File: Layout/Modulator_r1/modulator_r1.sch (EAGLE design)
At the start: 72 parts, among them Q1 FA-20H, U1 ATMEGA328P-AU, U2 TPS79933QDDCRQ1, U3 CC1125RHBT, U4 MCP1700T-3302E/TT, U5 FT232RL, U6 SIP32509DT-T1-GE3

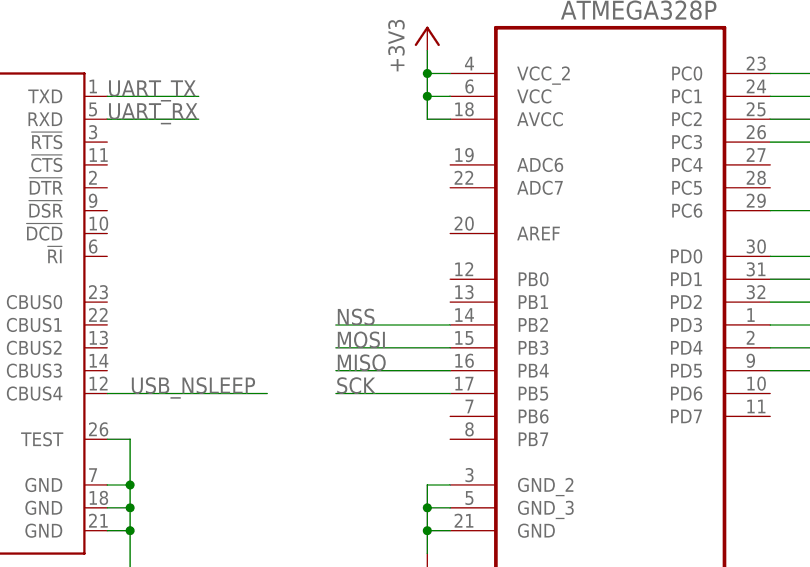
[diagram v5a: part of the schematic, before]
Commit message: Connected CC_Reset and GPIO0.
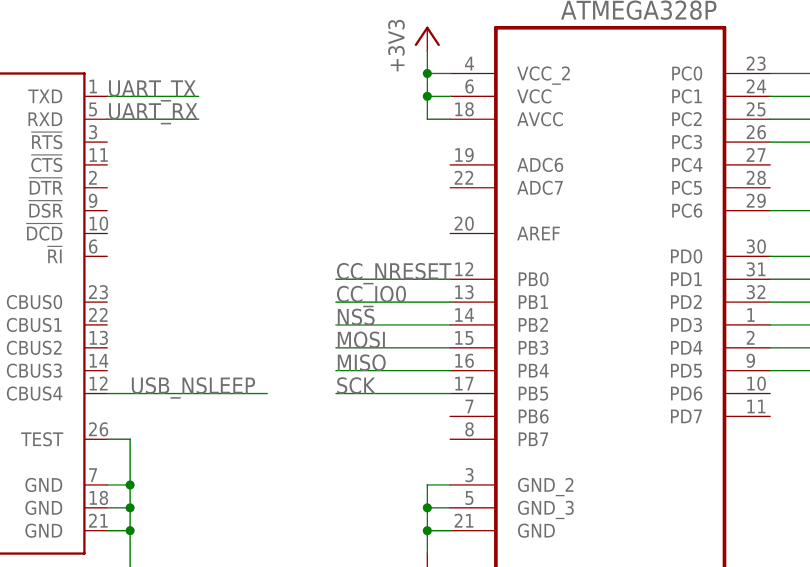
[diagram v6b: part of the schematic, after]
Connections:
- net CC_IO0: now also U1.PB1
- net CC_NRESET: now also U1.PB0
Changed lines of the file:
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@@
 <label x="162.56" y="58.42" size="1.778" layer="95"/>
+</segment>
+<segment>
+<pinref part="U1" gate="A" pin="PB1"/>
+<wire x1="25.4" y1="35.56" x2="12.7" y2="35.56" width="0.1524" layer="91"/>
+<label x="12.7" y="35.56" size="1.778" layer="95"/>
 </segment>
 </net>
@@
 <label x="162.56" y="40.64" size="1.778" layer="95"/>
 </segment>
+<segment>
+<pinref part="U1" gate="A" pin="PB0"/>
+<wire x1="25.4" y1="38.1" x2="12.7" y2="38.1" width="0.1524" layer="91"/>
+<label x="12.7" y="38.1" size="1.778" layer="95"/>
+</segment>
 </net>

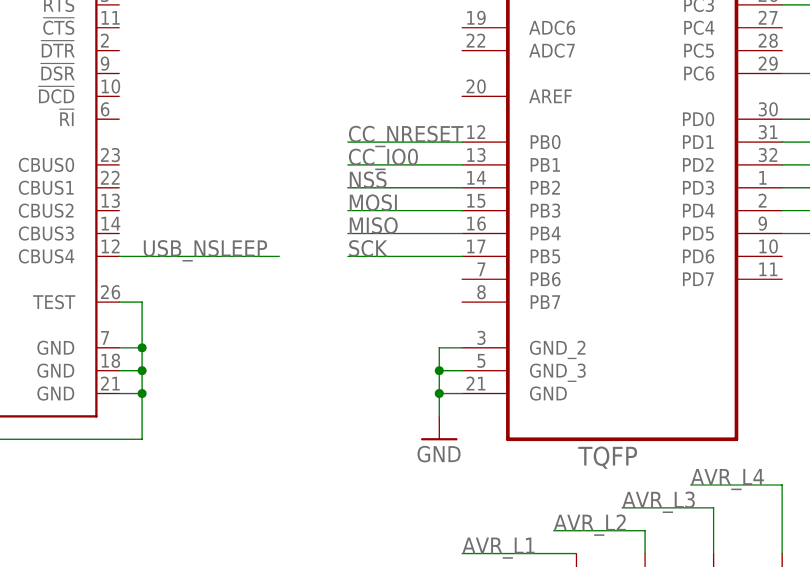
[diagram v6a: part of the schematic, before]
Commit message: Connect GPIO2/3.
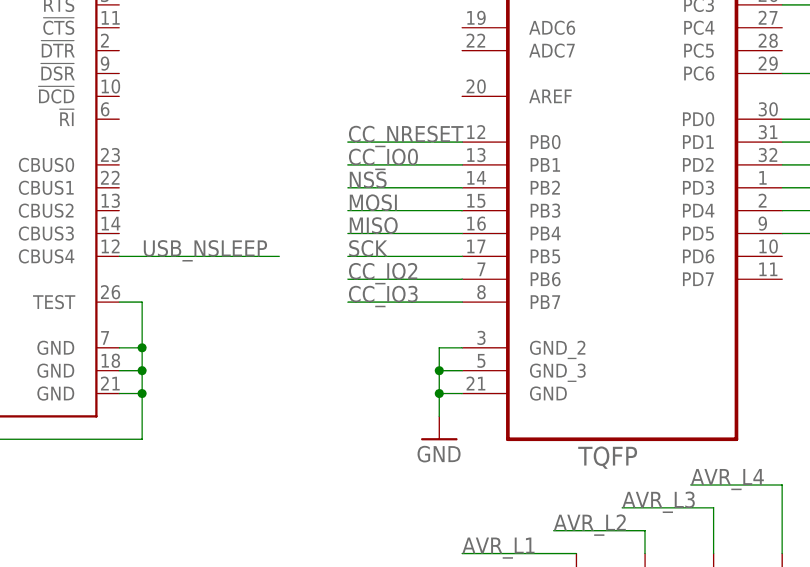
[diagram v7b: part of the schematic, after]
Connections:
- net CC_IO2: now also U1.PB6
- net CC_IO3: now also U1.PB7
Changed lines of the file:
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@@
 <label x="162.56" y="53.34" size="1.778" layer="95"/>
+</segment>
+<segment>
+<pinref part="U1" gate="A" pin="PB7"/>
+<wire x1="25.4" y1="20.32" x2="12.7" y2="20.32" width="0.1524" layer="91"/>
+<label x="12.7" y="20.32" size="1.778" layer="95"/>
 </segment>
 </net>
@@
 <label x="162.56" y="55.88" size="1.778" layer="95"/>
 </segment>
+<segment>
+<pinref part="U1" gate="A" pin="PB6"/>
+<wire x1="25.4" y1="22.86" x2="12.7" y2="22.86" width="0.1524" layer="91"/>
+<label x="12.7" y="22.86" size="1.778" layer="95"/>
+</segment>
 </net>

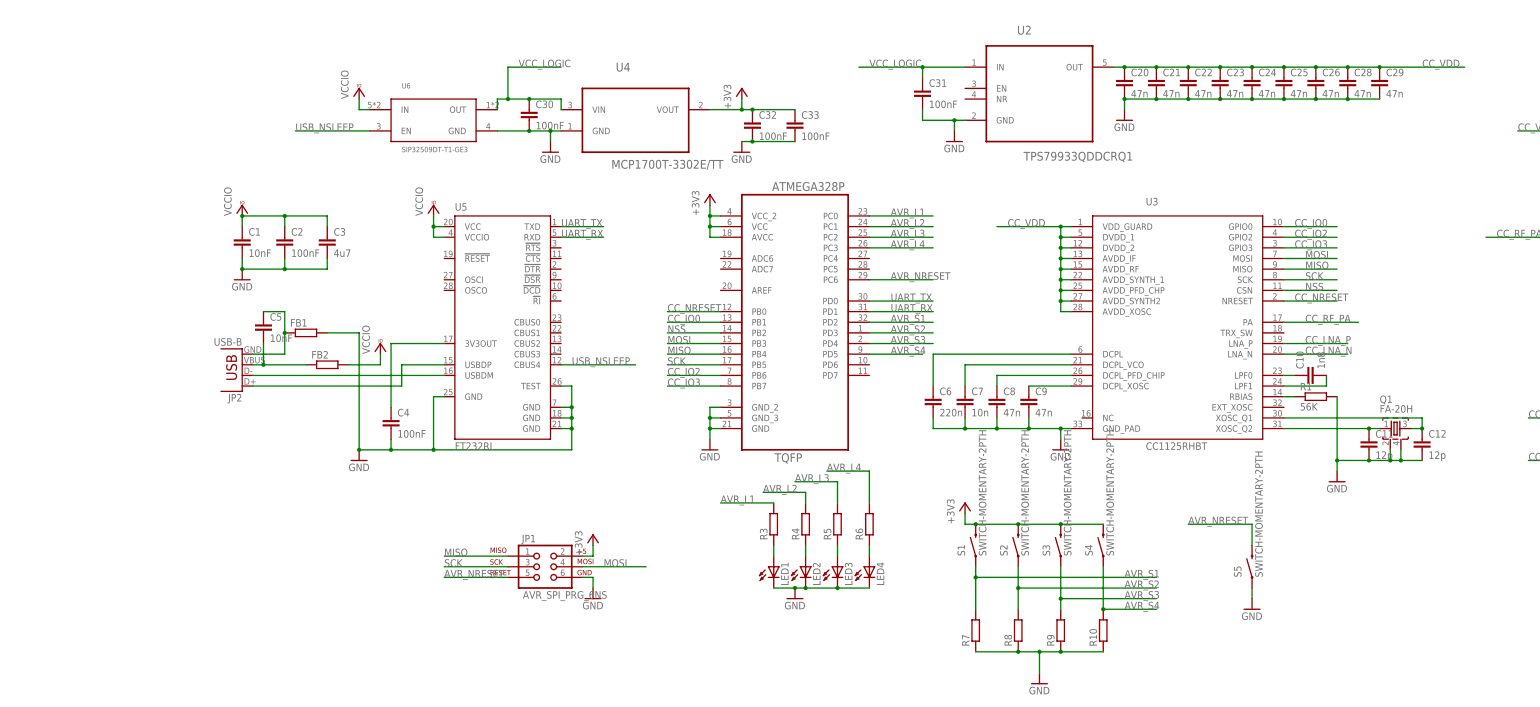
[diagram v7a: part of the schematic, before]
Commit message: Add test pads.
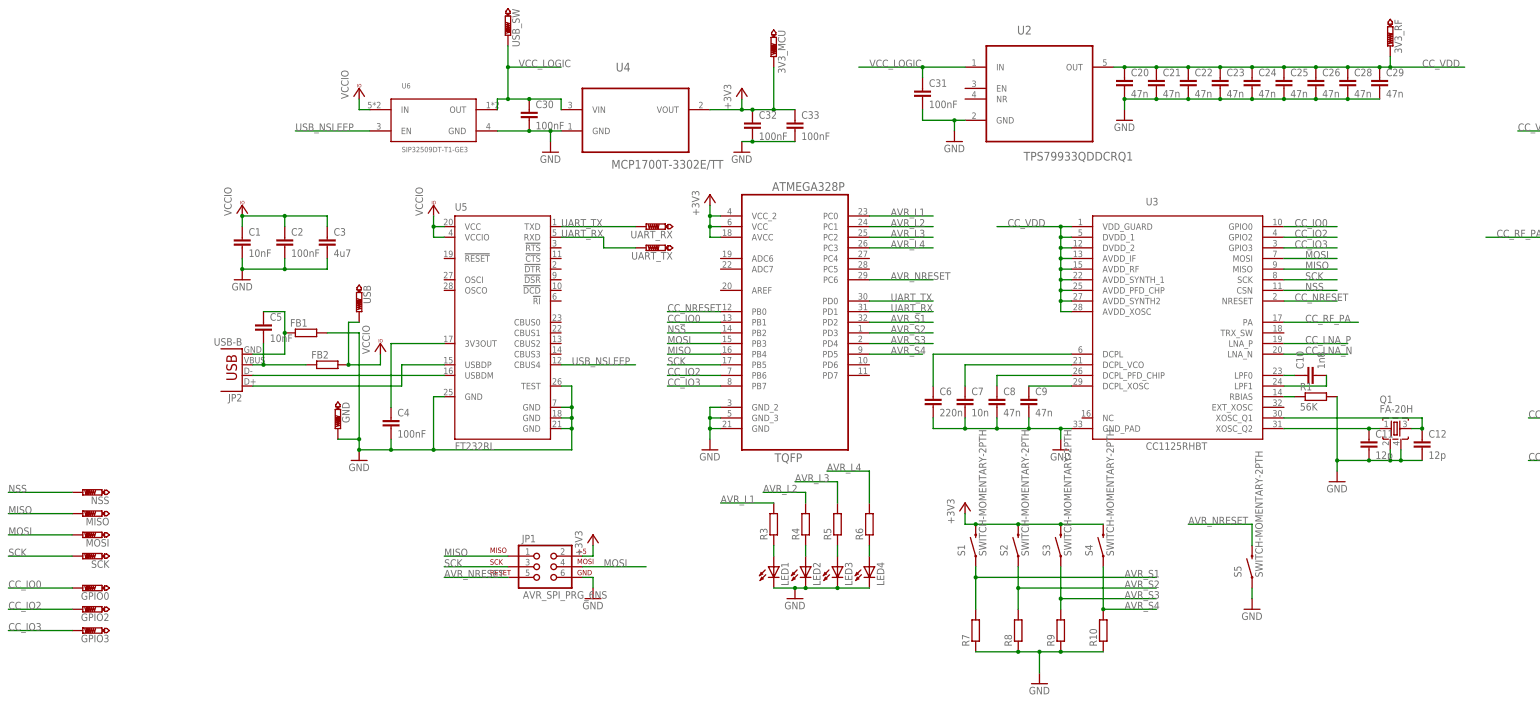
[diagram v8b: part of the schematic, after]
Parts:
- added 3V3_MCU, 3V3_RF, GND, USB, USB_SW: PTR1B2,54, testpad:PTR1B2,54
- added GPIO0, GPIO2, GPIO3, MISO, MOSI, NSS, SCK, UART_RX, UART_TX: PTR1B1,27, testpad:PTR1B1,27
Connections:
- net +3V3: now also 3V3_MCU.TP
- net CC_IO0: now also GPIO0.TP
- net CC_IO2: now also GPIO2.TP
- net CC_IO3: now also GPIO3.TP
- net CC_VDD: now also 3V3_RF.TP
- net GND: now also GND.TP
- net MISO: now also MISO.TP
- net MOSI: now also MOSI.TP
- net NSS: now also NSS.TP
- net SCK: now also SCK.TP
- net UART_RX: now also UART_TX.TP
- net UART_TX: now also UART_RX.TP
- net VCCIO: now also USB.TP
- net VCC_LOGIC: now also USB_SW.TP
